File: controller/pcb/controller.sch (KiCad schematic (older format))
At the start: 55 parts, among them J1 POWER, J2 10K POT, Q1 2N2222, Q12 TIP41, Q13 TIP41, Q15 2N2222, Q2 TIP42, Q3 TIP42, Q4 2N2222, Q5 2N2222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

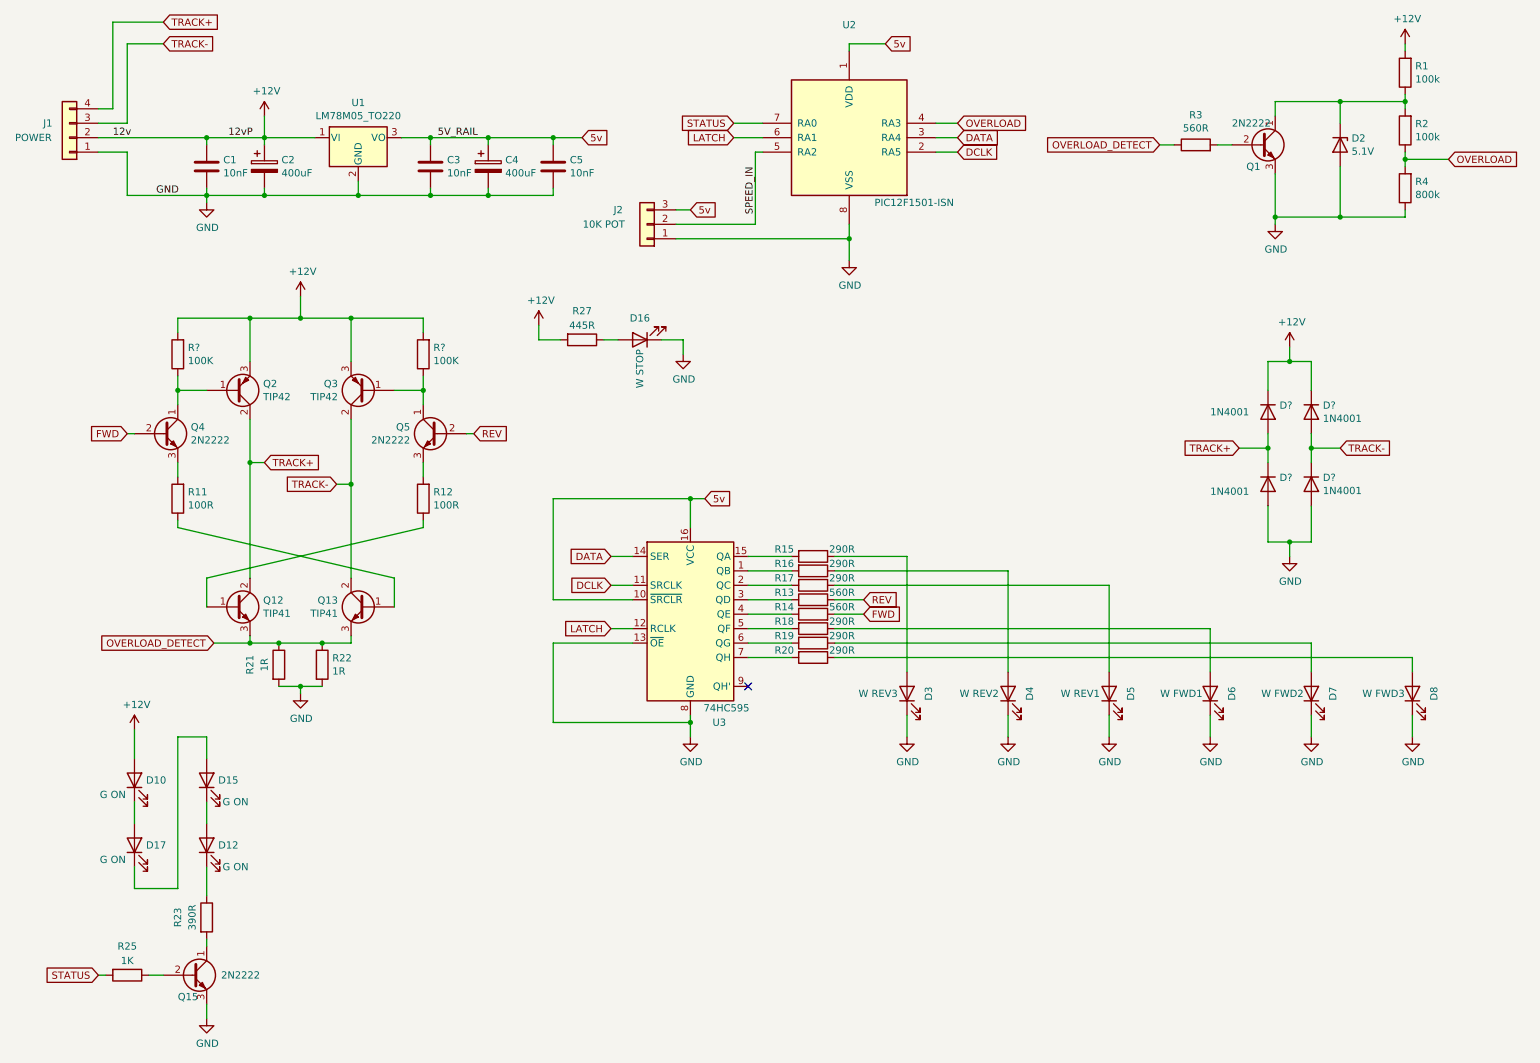
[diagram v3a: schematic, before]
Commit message: Added gradient control to PCB.
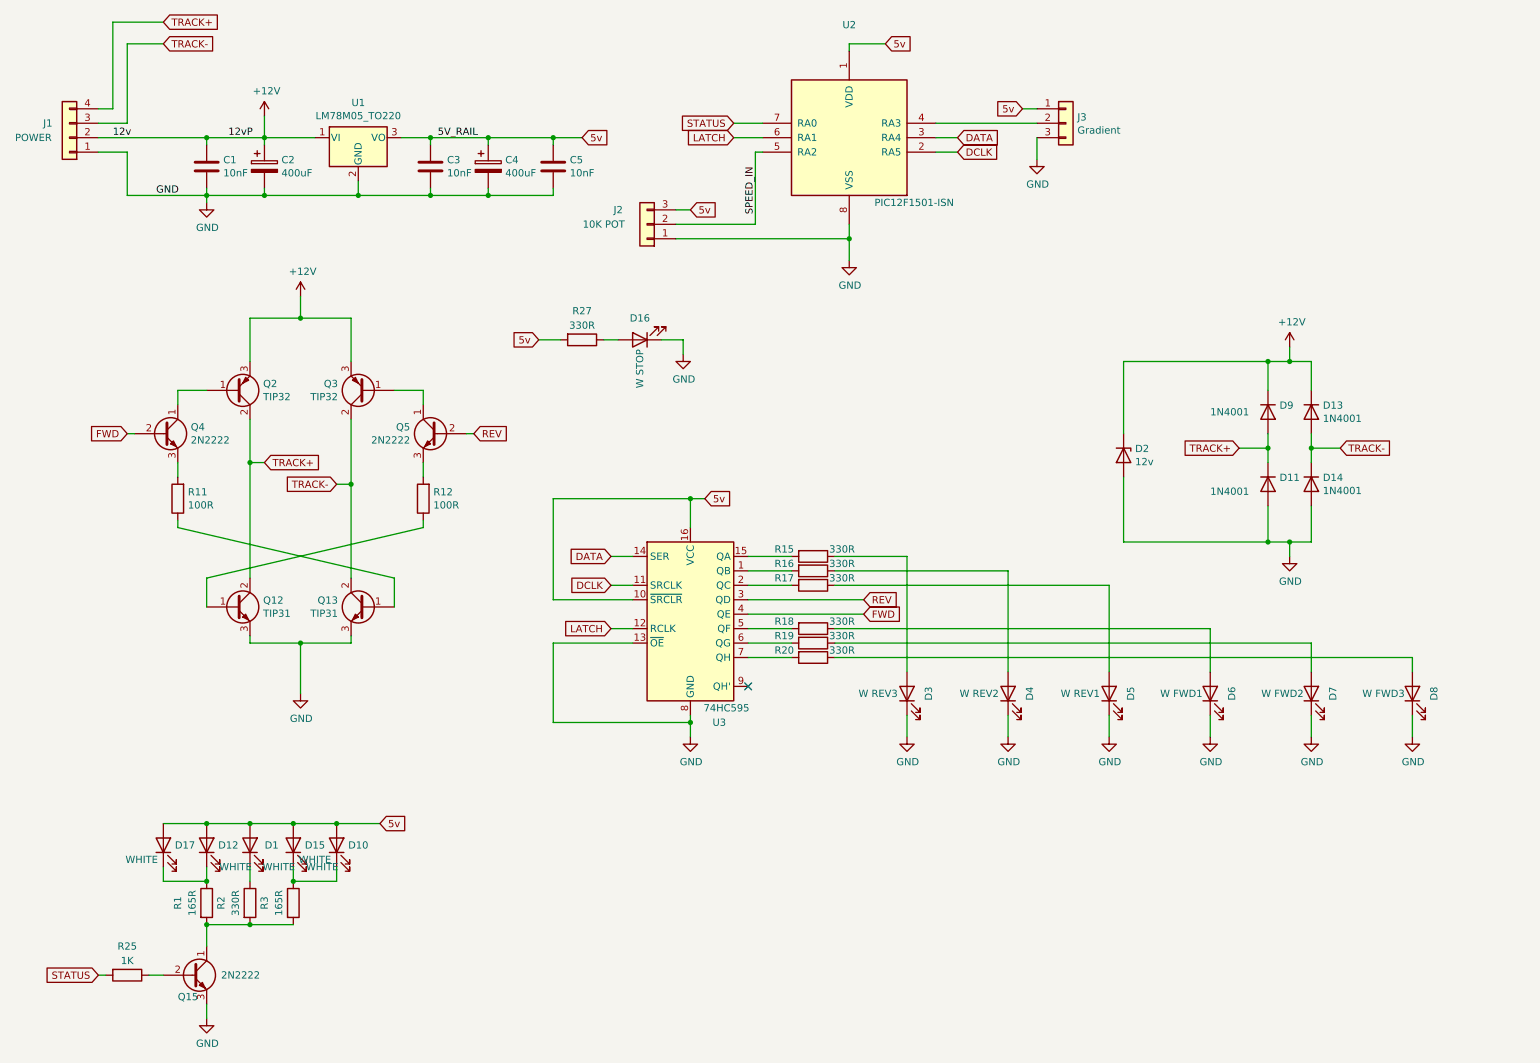
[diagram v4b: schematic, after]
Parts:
- removed Q1: 2N2222, TO_SOT_Packages_THT:TO-92_Inline_Wide, symbol Transistor_BJT:BC237
- removed R13, R14: 560R, Resistors_THT:R_Axial_DIN0411_L9.9mm_D3.6mm_P12.70mm_Horizontal, symbol Device:R
- removed R21, R22: 1R, Resistors_THT:R_Axial_DIN0614_L14.3mm_D5.7mm_P20.32mm_Horizontal, symbol Device:R
- removed R23: 390R, Resistors_THT:R_Axial_DIN0411_L9.9mm_D3.6mm_P12.70mm_Horizontal, symbol Device:R
- removed R4: 800k, Resistors_THT:R_Axial_DIN0411_L9.9mm_D3.6mm_P12.70mm_Horizontal, symbol Device:R
- removed R? (x2): 100K, Resistors_THT:R_Axial_DIN0411_L9.9mm_D3.6mm_P12.70mm_Horizontal, symbol Device:R
- added D1: WHITE, LEDs:LED_D5.0mm, symbol Device:LED
- added J3: Gradient, Pin_Headers:Pin_Header_Straight_1x03_Pitch2.54mm, symbol Connector_Generic:Conn_01x03
- D10, D12, D15, D17: value G ON -> WHITE
- D11, D13, D14, D9: renamed from D?; footprint (none) -> Diodes_THT:D_A-405_P7.62mm_Horizontal
- D2: value 5.1V -> 12v; footprint Diodes_THT:D_DO-41_SOD81_P7.62mm_Horizontal -> Diodes_THT:D_A-405_P7.62mm_Horizontal
- Q12, Q13: value TIP41 -> TIP31
- Q2, Q3: value TIP42 -> TIP32
- R1: value 100k -> 165R
- R15, R16, R17, R18, R19, R20: value 290R -> 330R
- R2: value 100k -> 330R
- R27: value 445R -> 330R
- R3: value 560R -> 165R
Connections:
- net +12V: now also D2.1 (K); no longer D10.2 (A), R1.2, R27.2
- net 5v: now also D10.2 (A), D12.2 (A), D15.2 (A), D17.2 (A), R27.2, D1.2 (A), J3.1 (Pin_1)
- net FWD: now also U3.4 (QE)
- net GND: now also Q12.3 (E), Q13.3 (E), J3.3 (Pin_3)
- net REV: now also U3.3 (QD)
- net at D12.1 (K): now also D17.1 (K), R1.1
- net at Q15.1 (C): now also R1.2, R2.2, R3.2
- net at D15.1 (K): now also D10.1 (K), R3.1; no longer D12.2 (A)
- net OVERLOAD: no longer names the net of U2.4 (RA3)
- net OVERLOAD: now also J3.2 (Pin_2); no longer R2.1
- removed net OVERLOAD_DETECT: Q12.3 (E), Q13.3 (E), R3.1
- new net: D1.1 (K), R2.1
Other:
- moved on the sheet: D10, D15, D17
